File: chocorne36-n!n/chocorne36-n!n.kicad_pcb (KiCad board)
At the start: 2 copper layers, 112 x 87.7 mm, 30 parts, among them SW10 SW_Push, SW11 SW_Push, SW12 SW_Push, SW14 SW_Push, SW15 SW_Push, SW16 SW_Push, SW17 SW_Push, SW18 SW_Push, SW2 SW_Push, SW20 SW_Push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

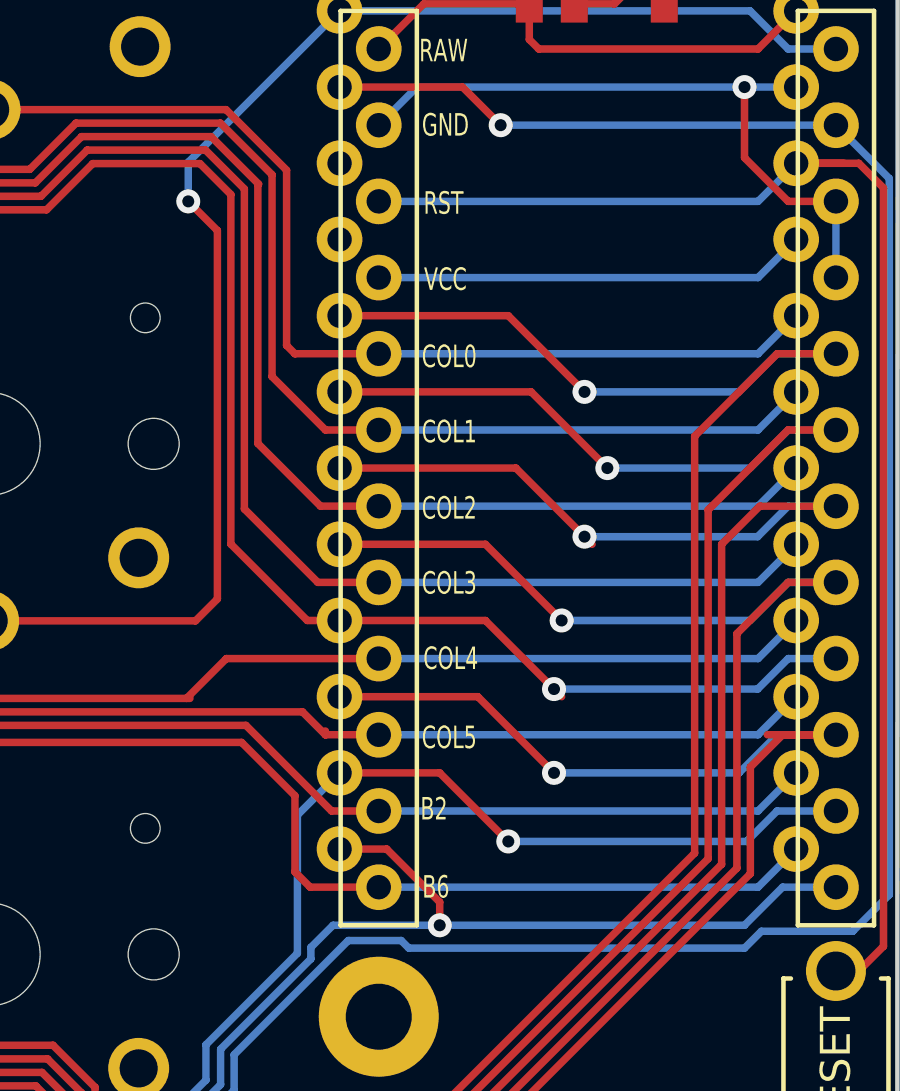
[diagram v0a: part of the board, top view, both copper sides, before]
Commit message: Change the silks for the controller.
Change the silks for the controller to avert future meltdowns about it.
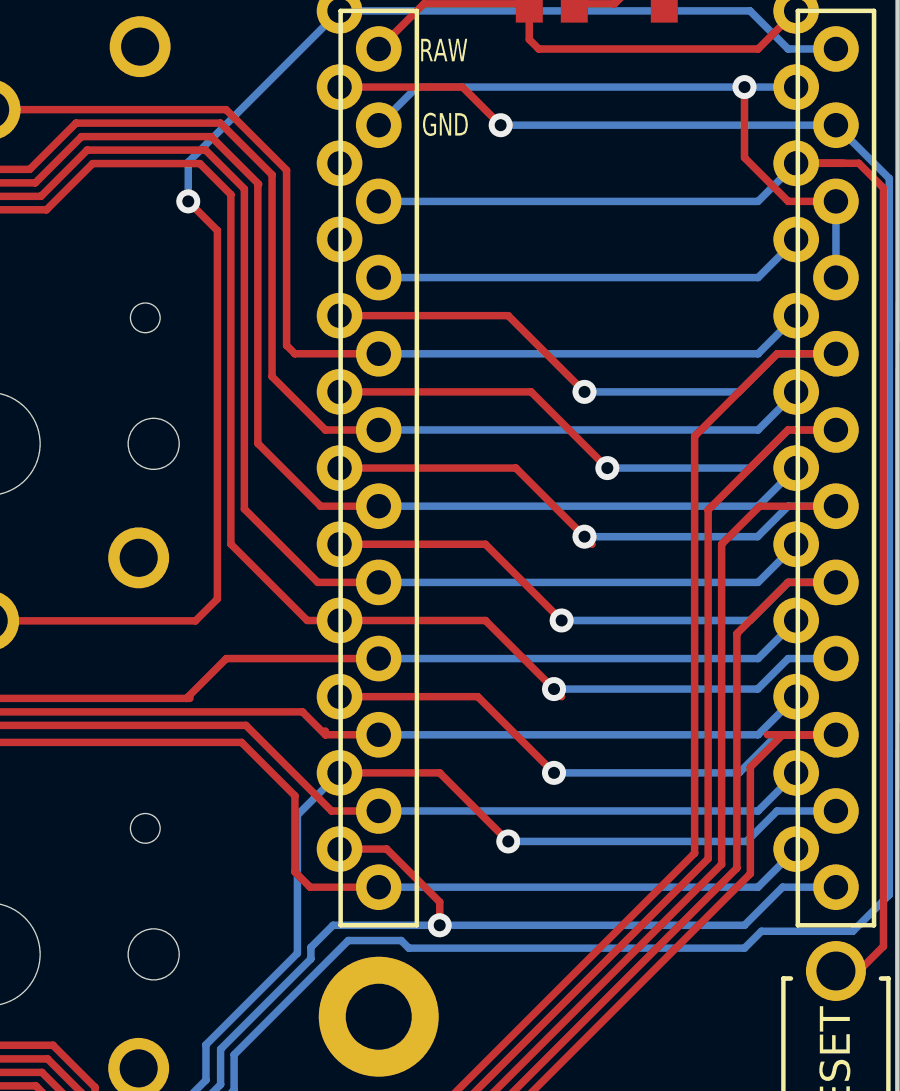
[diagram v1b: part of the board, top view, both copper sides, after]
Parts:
- U1: footprint kbd:ProMicro_v2 -> kbd:ProMicro_v2_1min
